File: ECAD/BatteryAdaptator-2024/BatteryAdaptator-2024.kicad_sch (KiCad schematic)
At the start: 6 parts, among them J1 USB3_A, J2 Conn_01x02

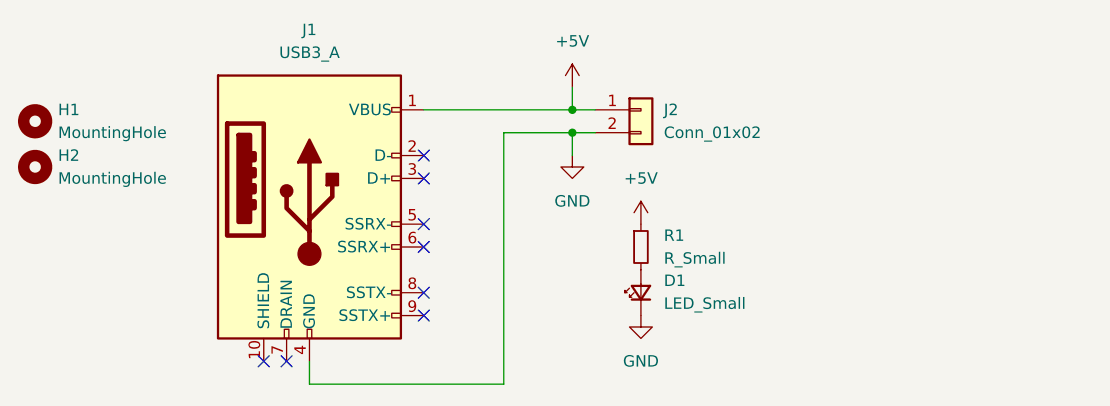
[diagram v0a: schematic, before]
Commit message: update live 177
- Conn USB lib
- Conn USB 3D
- Silkscreen
- Dimensions
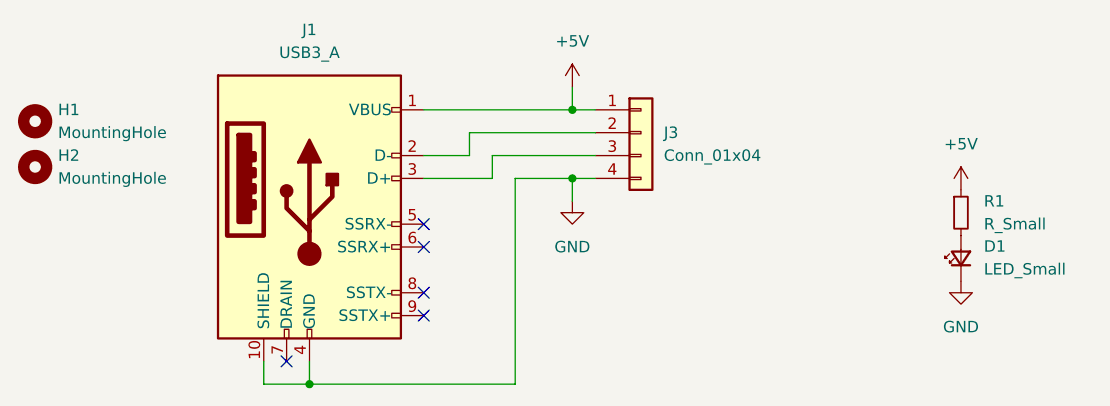
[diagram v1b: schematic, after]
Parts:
- removed J2: Conn_01x02, Connector_Molex:Molex_KK-396_5273-02A_1x02_P3.96mm_Vertical, symbol Connector_Generic:Conn_01x02
- added J3: Conn_01x04, Connector_PinHeader_2.54mm:PinHeader_1x04_P2.54mm_Vertical, symbol Connector_Generic:Conn_01x04
- J1: footprint (none) -> PAMI:USB A3.0 - PowerBank XHC-005
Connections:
- net +5V: now also J3.1 (Pin_1)
- net GND: now also J1.10 (SHIELD), J3.4 (Pin_4)
- net at J1.2 (D-): now also J3.2 (Pin_2)
- net at J1.3 (D+): now also J3.3 (Pin_3)
- no-connect marks 8 -> 5
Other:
- moved on the sheet: D1, R1
